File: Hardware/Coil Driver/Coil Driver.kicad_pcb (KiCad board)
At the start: 2 copper layers, 88 parts, among them J1 Barrel_Jack_Switch, J2 0.1" Header, J3 Tag-connect-NL, J4 0.1" Header, Q1 DMN3023L, Q2 DMN3023L, Q3 DMN3023L, Q4 DMN3023L, SW1 BTN_RST, SW2 BTN_USR1, SW3 BTN_USR2, U1 DGD05473, U2 MCP16331, U3 DGD05473, U4 STM32F070F6P6, Y1 8MHz

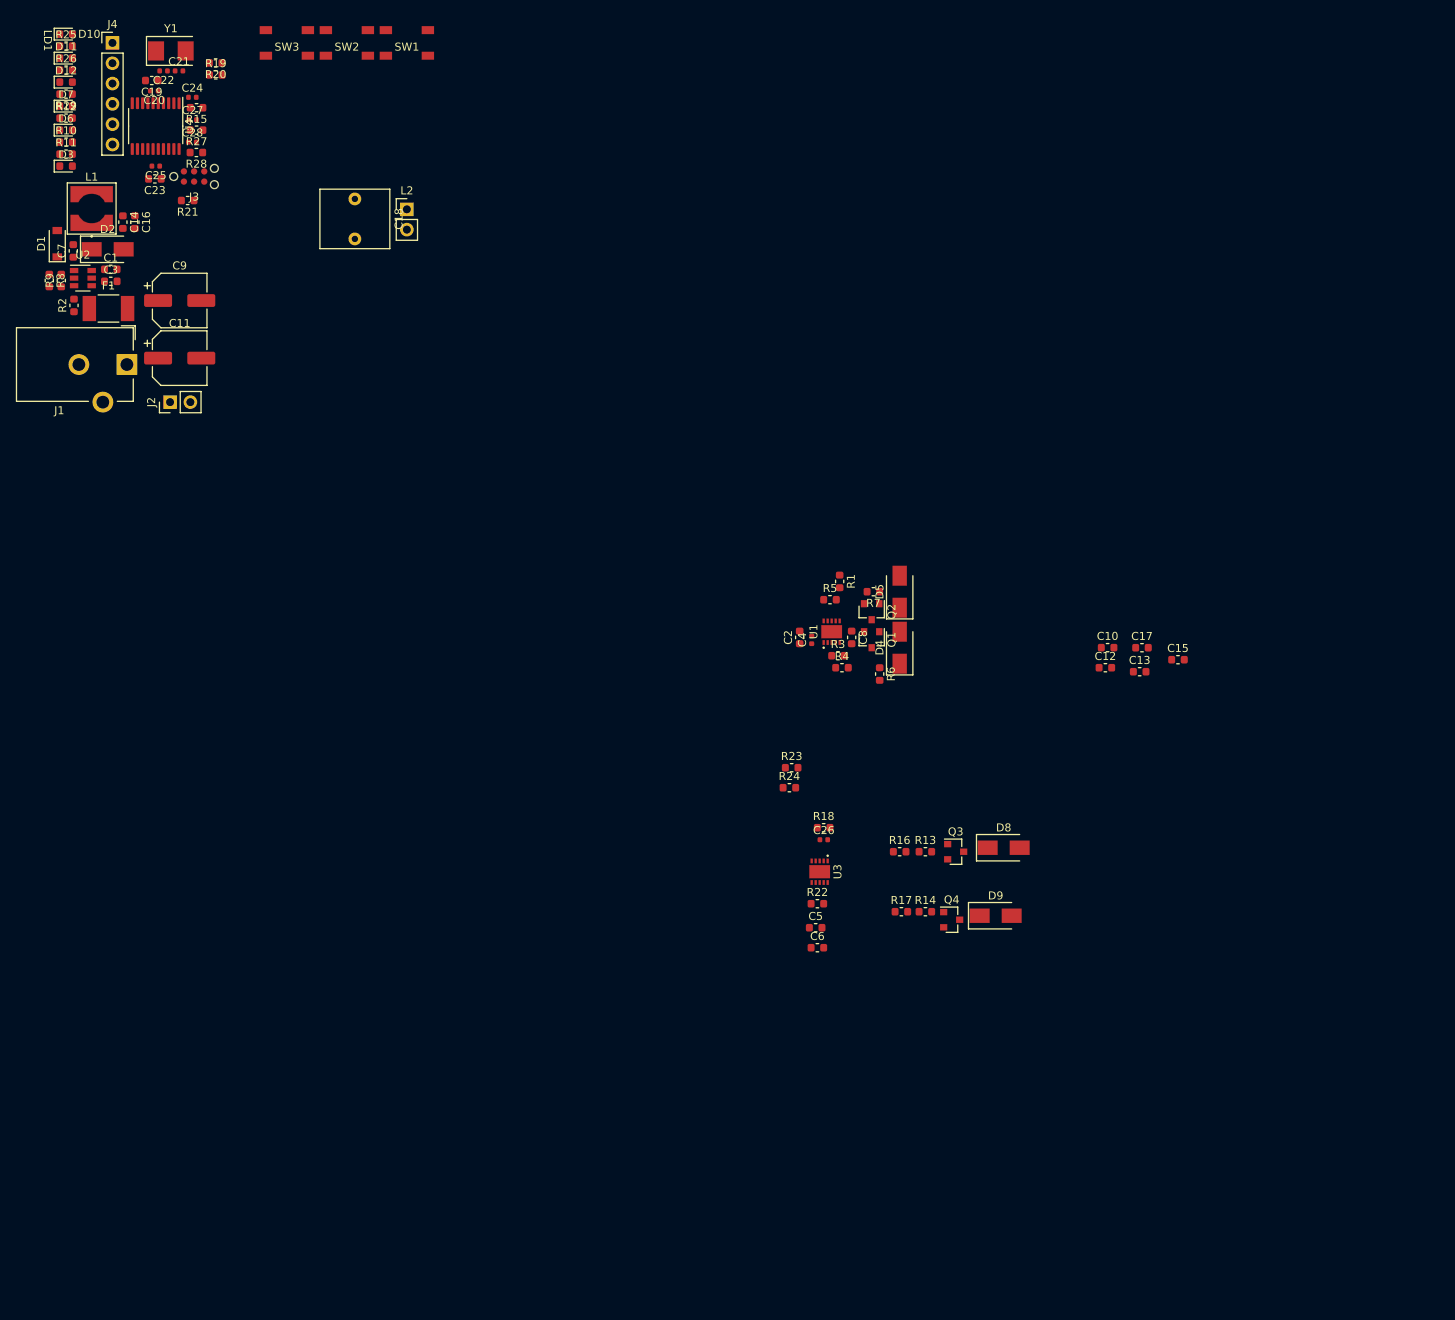
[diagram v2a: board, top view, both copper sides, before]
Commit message: completed first draft of part placement, and switching loop layout of gate drivers
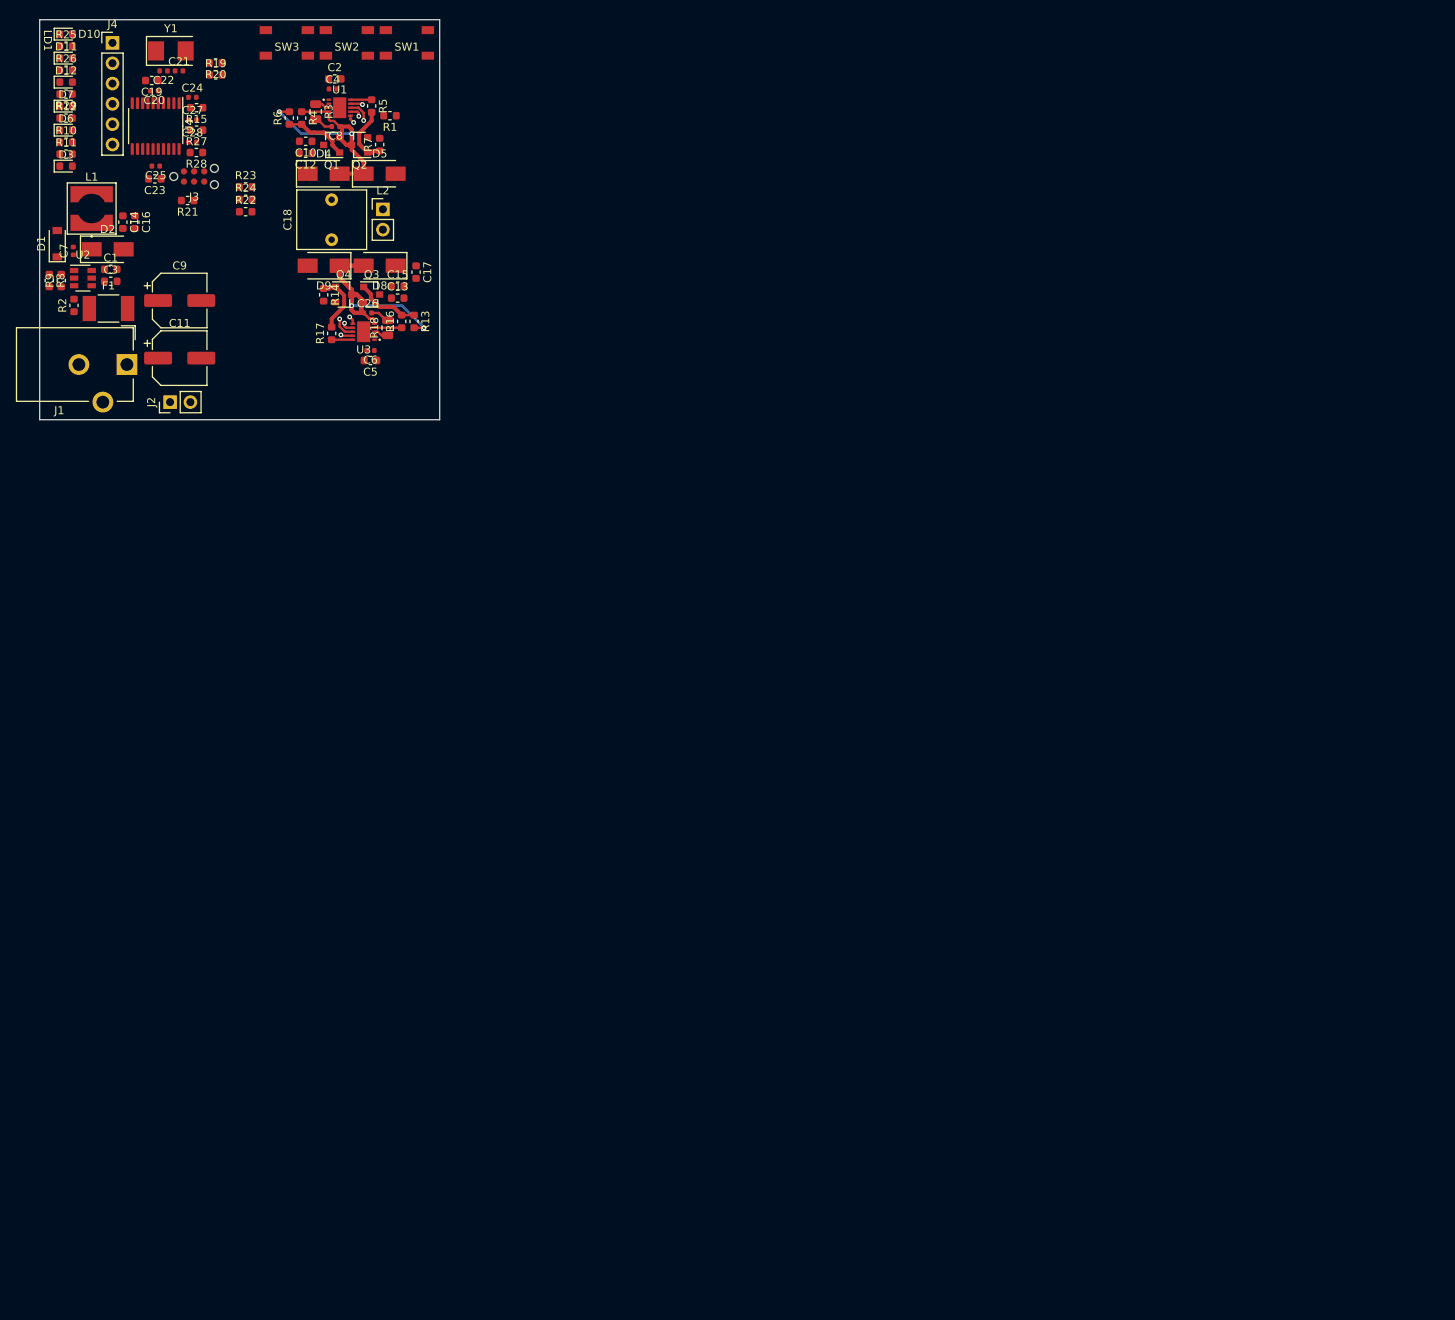
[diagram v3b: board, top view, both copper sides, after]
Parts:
- C6, C7, C8: footprint Capacitor_SMD:C_0603_1608Metric -> Capacitor_SMD:C_0402_1005Metric
- R18, R3: footprint Resistor_SMD:R_0603_1608Metric -> Resistor_SMD:R_0805_2012Metric
- moved C12 118.9 mm to (45.2, 28.7), turned to 180 degrees
- moved C10 118.5 mm to (45.2, 27.2), turned to 180 degrees
- moved D9 116.9 mm to (47.5, 42.8), turned to 180 degrees
- moved R22 112.2 mm to (37.8, 36.0)
- moved Q4 109.0 mm to (50.0, 46.4)
- moved C15 108.1 mm to (56.8, 45.3)
- moved R14 107.7 mm to (47.5, 46.4), turned to 270 degrees
- moved D8 106.7 mm to (54.5, 42.8), turned to 180 degrees
- moved C13 103.8 mm to (56.8, 46.8)
- moved C17 102.2 mm to (59.0, 43.5), turned to 270 degrees
- moved R17 101.5 mm to (48.5, 51.2), turned to 90 degrees
- moved R6 101.4 mm to (43.2, 24.3), turned to 90 degrees
- moved Q3 100.9 mm to (53.5, 46.4)
- moved R24 100.1 mm to (37.8, 34.5)
- moved R23 99.6 mm to (37.8, 32.9)
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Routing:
- net /VSW-: track 0.00 -> 44.7 mm, vias 0 -> 2
- net /VSW+: track 0.00 -> 28.1 mm, vias 0 -> 2
- net Net-(Q3-Pad1): track 0.00 -> 8.07 mm
- net Net-(Q1-Pad1): track 0.00 -> 8.07 mm
- net Net-(Q2-Pad1): track 0.00 -> 7.68 mm
- net Net-(Q4-Pad1): track 0.00 -> 7.68 mm
- net /LIN: track 0.00 -> 5.74 mm, vias 0 -> 2
- net /HO_B: track 0.00 -> 3.40 mm
- net /HO_A: track 0.00 -> 3.40 mm
- net GND: track 0.00 -> 3.09 mm, vias 0 -> 2
- net /HIN: track 0.00 -> 3.00 mm, vias 0 -> 2
- net /LO_B: track 0.00 -> 2.65 mm
- net /LO_A: track 0.00 -> 2.65 mm
- net Net-(C26-Pad2): track 0.00 -> 2.40 mm
- net Net-(C8-Pad2): track 0.00 -> 2.40 mm
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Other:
- board outline added: 50 x 50 mm
- copper layers 2 -> 4
- net class Default: clearance 0.2 -> 0.1524; trace_width 0.25 -> 0.1524; via_dia 0.8 -> 0.6; via_drill 0.4 -> 0.3
- rule trace_clearance: 0.2 -> 0.1524
- rule trace_min: 0.2 -> 0.1524

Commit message: Added internal layers, routed power input and buck converter, and repositioned a few components. Defined PCB shape and moved to center of drawing template.
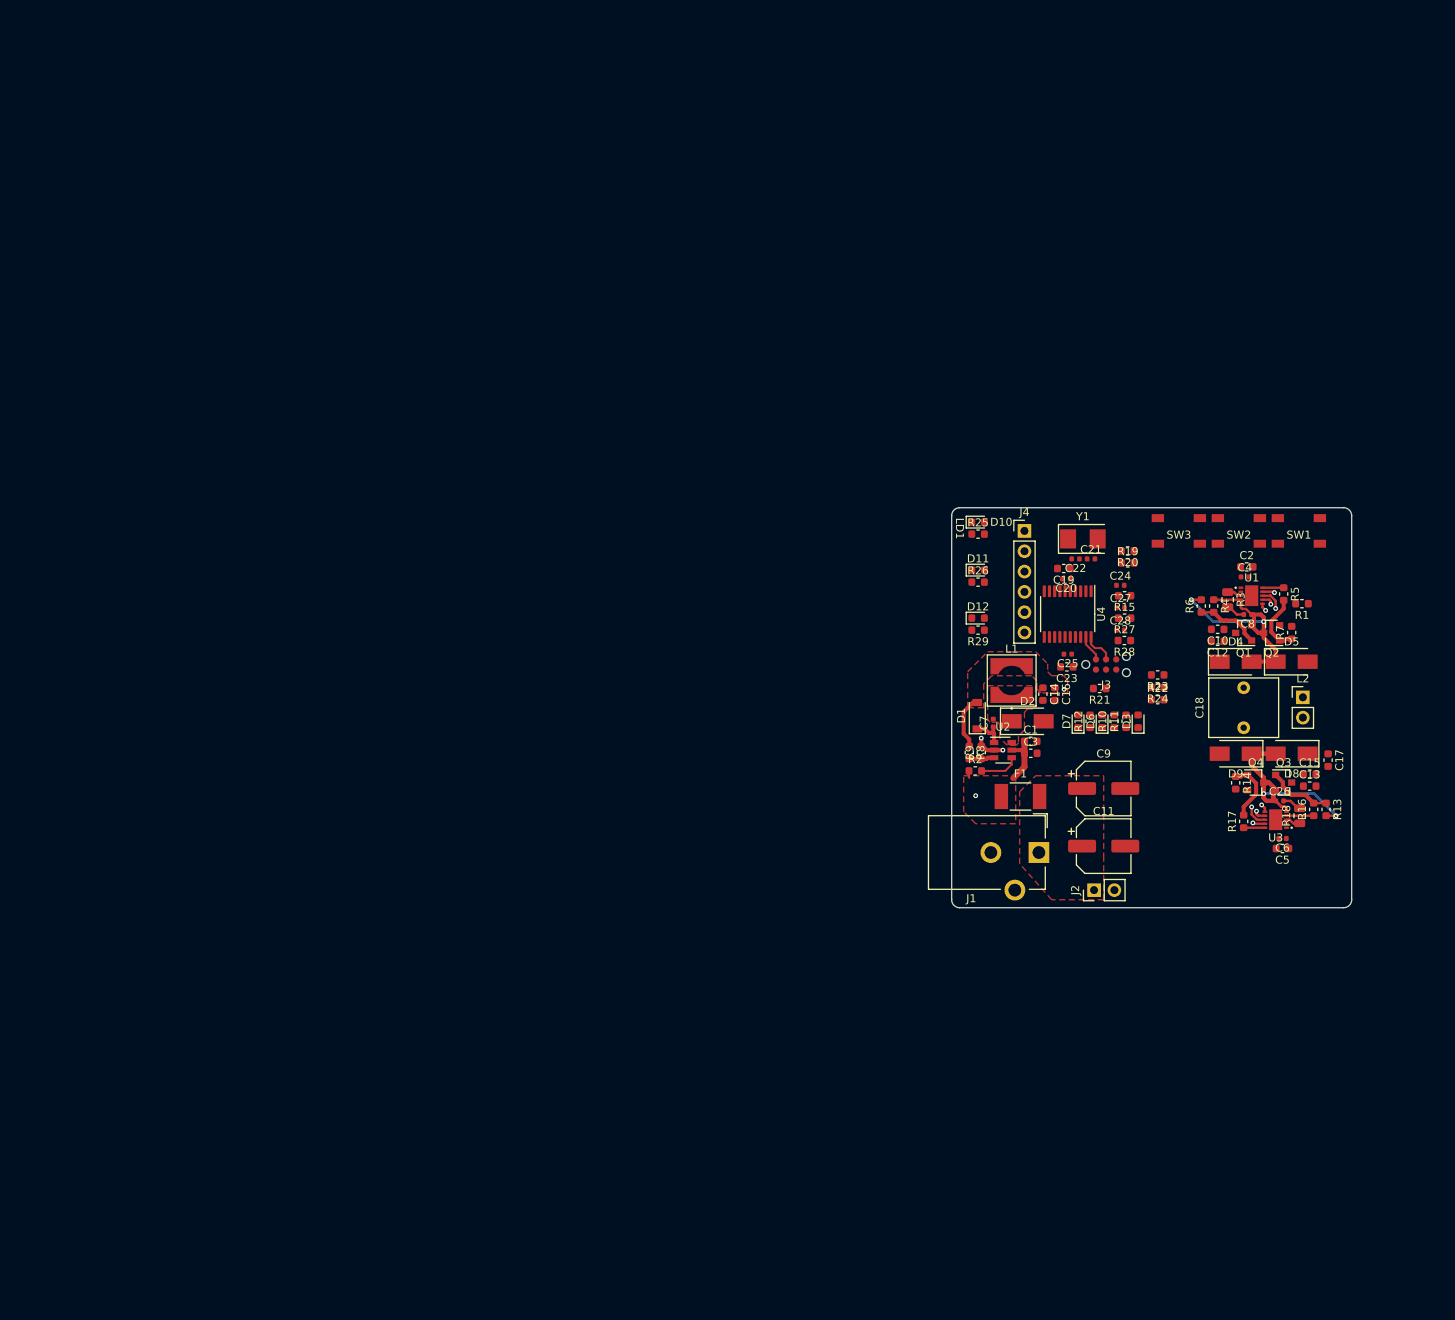
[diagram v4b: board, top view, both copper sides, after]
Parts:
- moved D3 150.9 mm to (149.3, 99.7), turned to 90 degrees
- moved R11 150.3 mm to (147.8, 99.7), turned to 90 degrees
- moved R10 149.7 mm to (146.3, 99.7), turned to 90 degrees
- moved D6 149.1 mm to (144.8, 99.7), turned to 90 degrees
- moved R12 148.6 mm to (143.3, 99.7), turned to 90 degrees
- moved D7 148.0 mm to (141.8, 99.7), turned to 90 degrees
- moved D12 132.2 mm to (129.3, 86.8)
- moved R29 132.2 mm to (129.3, 88.3)
- moved C24 131.1 mm to (147.1, 82.7)
- moved C27 131.1 mm to (147.1, 85.5)
- moved C28 131.1 mm to (147.1, 88.3)
- moved R15 131.1 mm to (147.6, 84.0)
- moved R27 131.1 mm to (147.6, 86.8)
- moved R28 131.1 mm to (147.6, 89.6)
- moved D11 130.7 mm to (129.3, 80.8)
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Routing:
- net +12V: track 0.00 -> 7.78 mm, vias 0 -> 1
- net +3V3: track 0.00 -> 6.78 mm, vias 0 -> 1
- net Net-(R2-Pad2): track 0.00 -> 4.94 mm
- net Net-(C7-Pad1): track 0.00 -> 4.21 mm
- net /SWCLK: track 0.00 -> 4.05 mm
- net GND: track 3.09 -> 7.00 mm, vias 2 -> 4
- net /SWDIO: track 0.00 -> 3.32 mm
- net Net-(R8-Pad2): track 0.00 -> 3.16 mm
- added copper zone on F.Cu, net +12V
- added copper zone on PWR.Cu, net +12V
- added copper zone on F.Cu, net +3V3
- added copper zone on PWR.Cu, net +3V3
- added copper zone on GND.Cu, net GND
- added copper zone on F.Cu, net Net-(C7-Pad2)
- added copper zone on F.Cu, net VDD
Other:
- outline, holes or cut-outs redrawn

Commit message: Done with initial routing of microcontroller. Flipped order of extra IO exposed on header to ease routing. Added some power pours
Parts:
- L2: footprint Connector_PinHeader_2.54mm:PinHeader_1x02_P2.54mm_Vertical -> Connector_PinSocket_2.54mm:PinSocket_1x02_P2.54mm_Vertical
- moved R21 16.5 mm to (148.3, 79.6)
- moved J3 8.94 mm to (150.0, 85.0), turned to 90 degrees
- moved R23 6.27 mm to (145.6, 92.5)
- moved R24 6.27 mm to (145.6, 94.1)
- moved R22 6.27 mm to (145.6, 95.7), turned to 180 degrees
- moved R19 4.31 mm to (148.3, 75.6), turned to 180 degrees
- moved R11 4.00 mm to (151.8, 99.7)
- moved C24 1.90 mm to (145.2, 82.7)
- moved C27 1.90 mm to (145.2, 85.5)
- moved C28 1.90 mm to (145.2, 88.3)
- moved R15 1.90 mm to (145.7, 84.0)
- moved R27 1.90 mm to (145.7, 86.8)
- moved R28 1.90 mm to (145.7, 89.6)
- moved R10 1.50 mm to (147.8, 99.7)
- moved D6 1.00 mm to (145.8, 99.7)
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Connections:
- net Net-(J4-Pad5) renamed /EX2
- J4 pad 4: Net-(J4-Pad4) -> /EX3
- J4 pad 6: Net-(J4-Pad6) -> /EX1
- U4 pad 12: Net-(J4-Pad4) -> /EX1
- U4 pad 17: Net-(J4-Pad6) -> /EX3
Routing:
- net Net-(C24-Pad1): track 0.00 -> 44.5 mm, vias 0 -> 2
- net Net-(C27-Pad1): track 0.00 -> 36.1 mm, vias 0 -> 2
- net Net-(C28-Pad1): track 0.00 -> 32.2 mm, vias 0 -> 2
- net /LD1: track 0.00 -> 15.4 mm
- net /GD_EN: track 2.03 -> 17.0 mm, vias 2 -> 4
- net /LD3: track 0.00 -> 13.7 mm
- net /LD2: track 0.00 -> 13.1 mm
- net Net-(R24-Pad2): track 0.00 -> 11.2 mm, vias 0 -> 2
- net Net-(R19-Pad2): track 0.00 -> 9.96 mm
- net /EX3: track 0.00 -> 9.82 mm
- net /SWDIO: track 3.32 -> 13.0 mm
- net Net-(J3-Pad3): track 0.00 -> 8.95 mm
- net /SWCLK: track 4.05 -> 12.7 mm
- net Net-(C21-Pad1): track 0.00 -> 8.61 mm
- net Net-(C22-Pad1): track 0.00 -> 8.59 mm
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
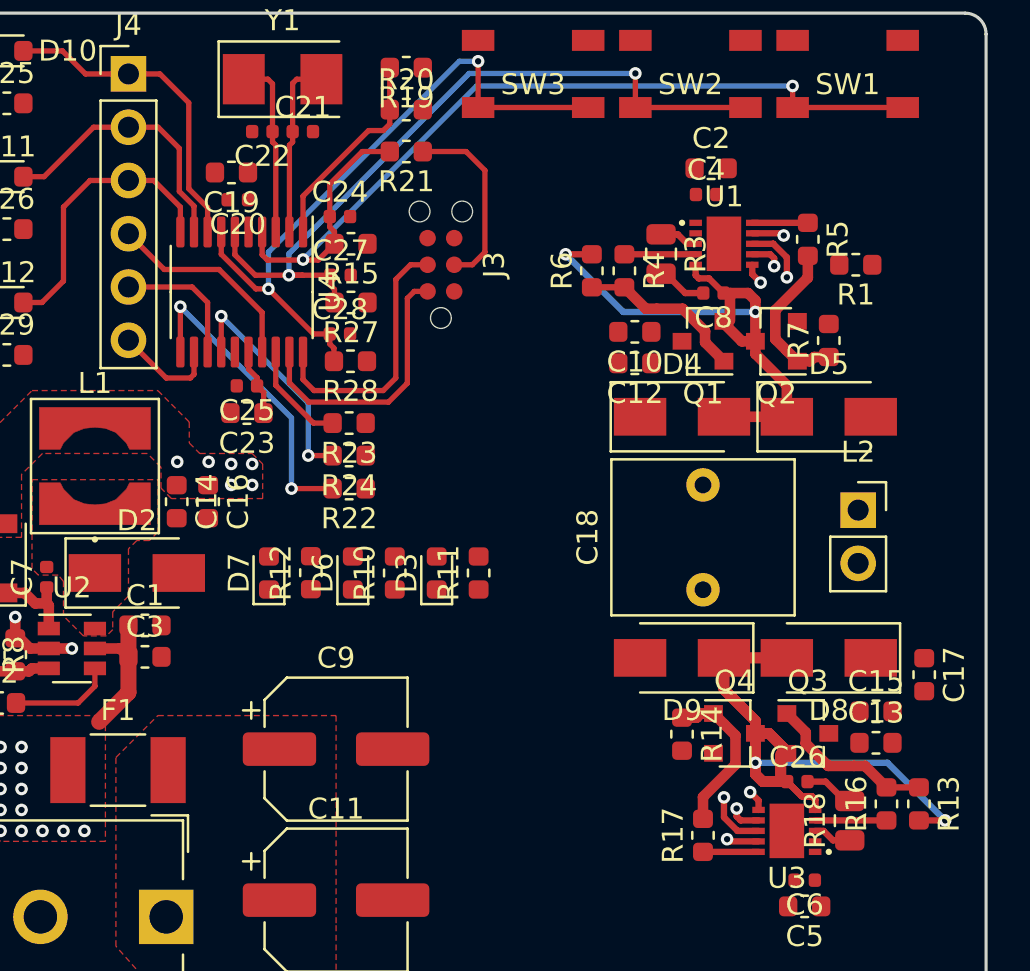
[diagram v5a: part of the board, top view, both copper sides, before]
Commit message: done with routing other than a few power/ground connections
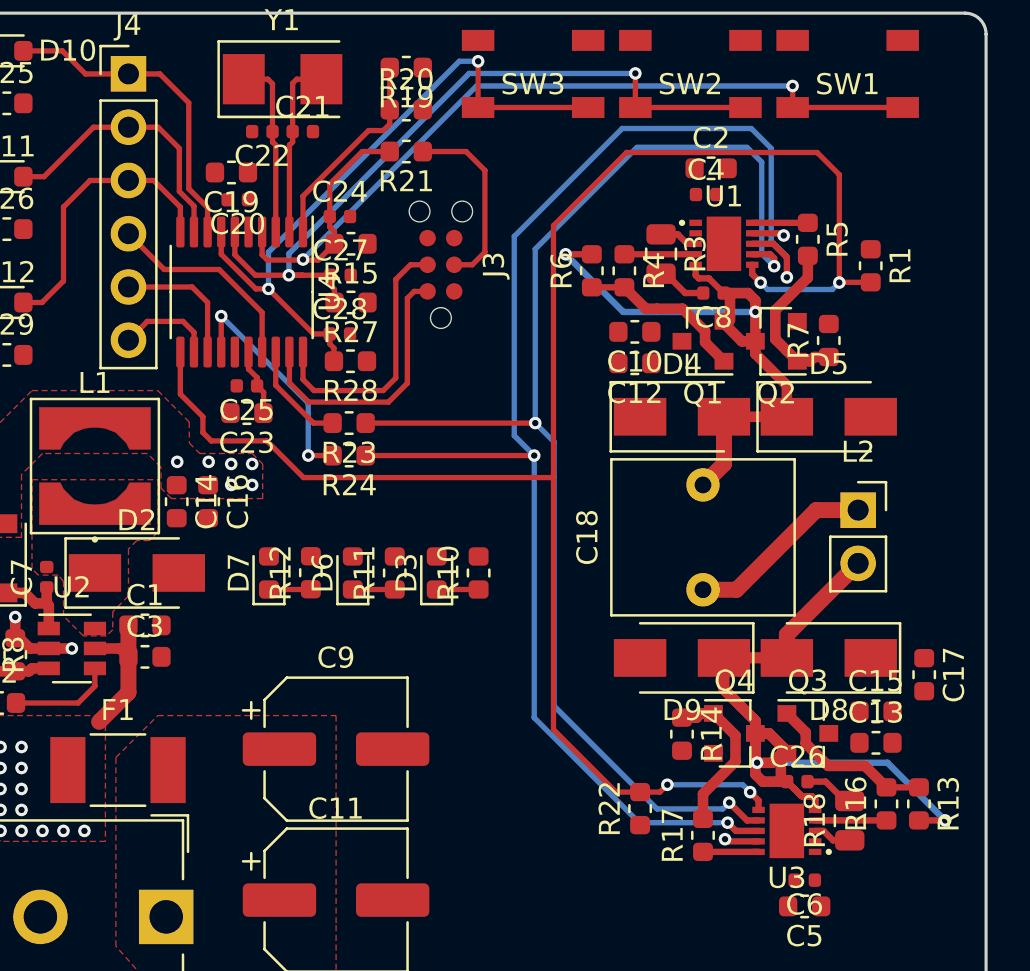
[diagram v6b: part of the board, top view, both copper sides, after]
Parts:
- moved R22 20.6 mm to (159.5, 110.9), turned to 90 degrees
- moved R10 4.00 mm to (151.8, 99.7)
- moved R11 4.00 mm to (147.8, 99.7)
- moved R1 0.71 mm to (170.5, 85.0), turned to 270 degrees
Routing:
- net /GD_EN: track 17.0 -> 86.5 mm
- net /LIN: track 5.74 -> 68.4 mm, vias 2 -> 3
- net /HIN: track 3.00 -> 62.3 mm, vias 2 -> 3
- net Net-(C18-Pad1): track 0.00 -> 8.97 mm
- net /VSW-: track 44.7 -> 48.7 mm
- net /VSW+: track 28.1 -> 31.7 mm
- net Net-(D7-Pad1): track 0.00 -> 2.01 mm
- net Net-(D6-Pad1): track 0.00 -> 2.00 mm
- net Net-(D3-Pad1): track 0.00 -> 2.00 mm
